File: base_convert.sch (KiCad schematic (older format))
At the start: 14 parts, among them J1 ISP, J2 DEBUG, Q1 Q_PMOS_GSD, SW2 SELECT, U1 MIC5317-3.3YM5-TR, U2 MSP430FR2033IPMR

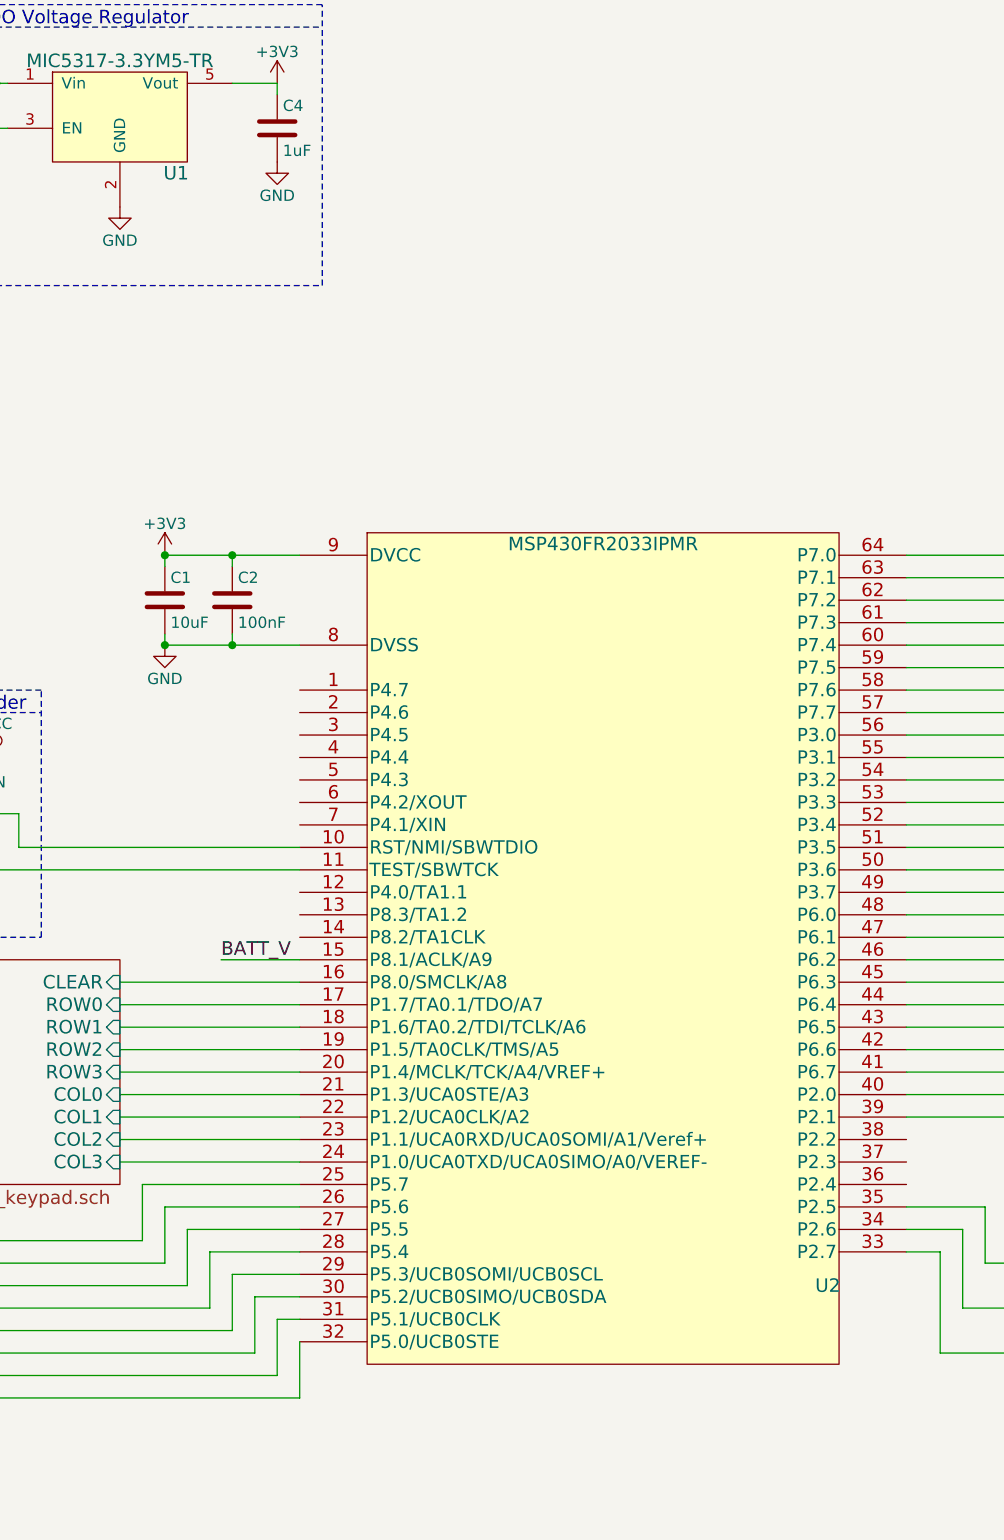
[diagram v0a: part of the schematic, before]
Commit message: spaw reference so U1 is uC as in previous version
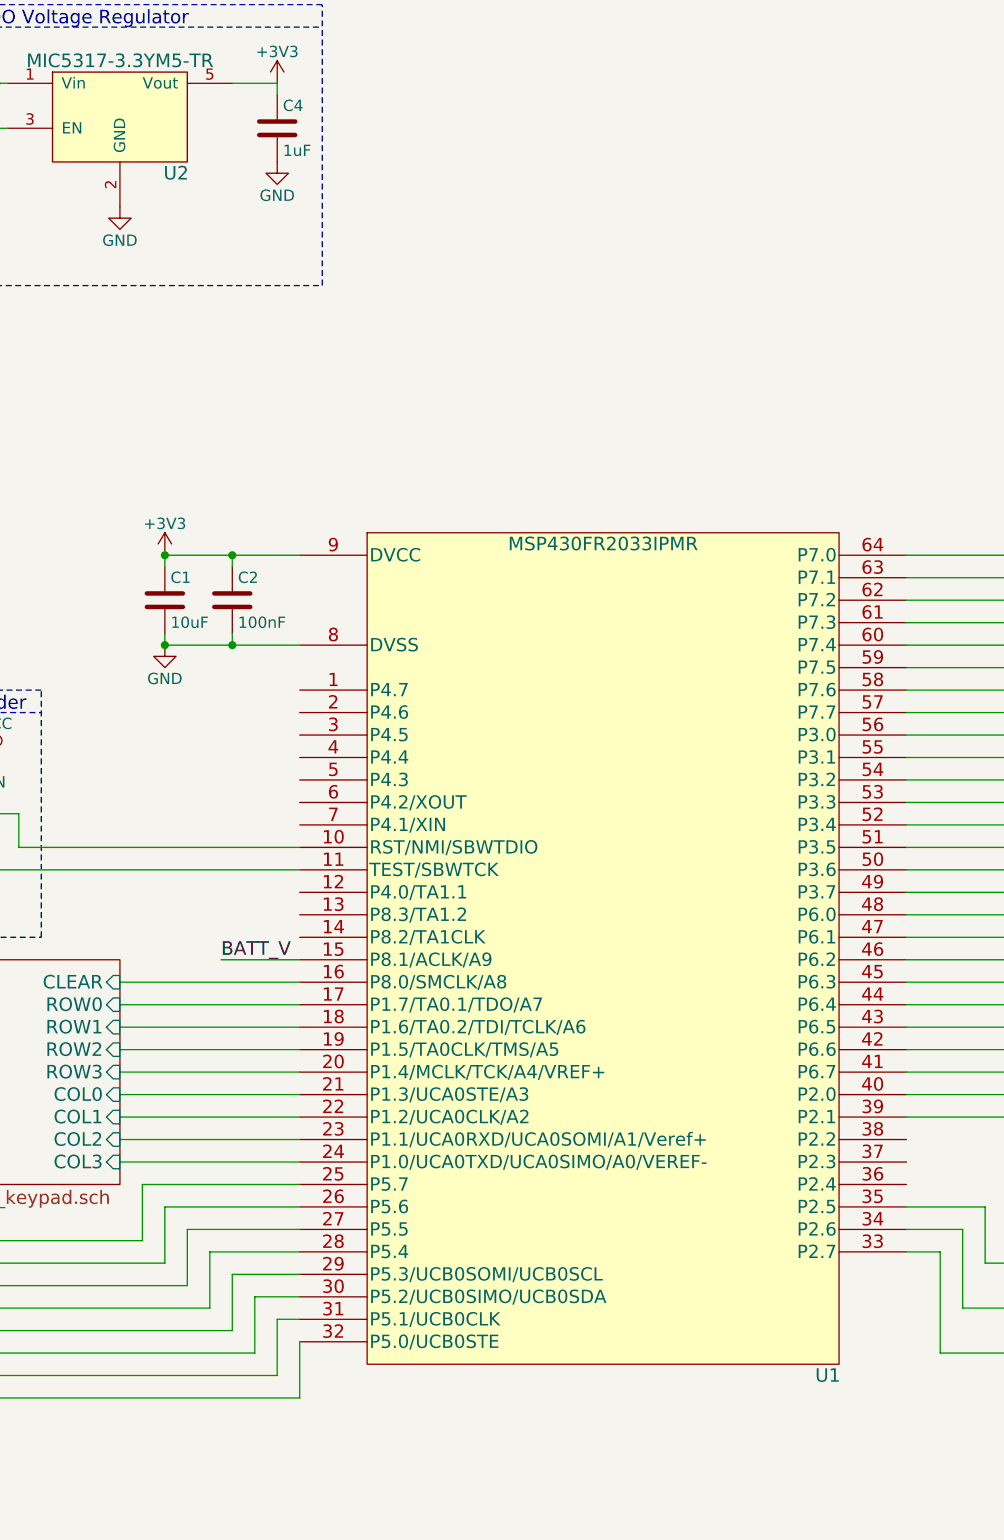
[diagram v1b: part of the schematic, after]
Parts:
- renumbered U2 to U1, U1 to U2
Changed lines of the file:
@@
 $EndComp
 $Comp
-L MSP430FR2033IPMR U2
+L MSP430FR2033IPMR U1
 U 1 1 5B2ADB04
 P 5050 3000
-F 0 "U2" H 7400 -250 60  0000 C CNN
+F 0 "U1" H 7400 -650 60  0000 C CNN
 F 1 "MSP430FR2033IPMR" H 6400 3050 60  0000 C CNN
 F 2 "Housings_QFP:LQFP-64_10x10mm_Pitch0.5mm" H 6400 3150 60  0001 C CNN
@@
 $EndComp
 $Comp
-L MIC5317 U1
+L MIC5317 U2
 U 1 1 5B283B2B
 P 4250 900
-F 0 "U1" H 4500 500 60  0000 C CNN
+F 0 "U2" H 4500 500 60  0000 C CNN
 F 1 "MIC5317-3.3YM5-TR" H 4250 1000 60  0000 C CNN
 F 2 "TO_SOT_Packages_SMD:SOT-23-5" H 4250 900 60  0001 C CNN
 F 3 "http://www.microchip.com/mymicrochip/filehandler.aspx?ddocname=en579427" H 4250 900 60  0001 C CNN
-F 4 "IC REG LINEAR 3.3V 150MA SOT23-5" H 4250 900 60  0001 C CNN "Description"
-F 5 "Microchip Technology" H 4250 900 60  0001 C CNN "Manufacture"
-F 6 "MIC5317-3.3YM5-TR" H 4250 900 60  0001 C CNN "Mfg Part Number"
-F 7 "SOT23-5" H 4250 900 60  0001 C CNN "Package"
+F 4 "Microchip Technology" H 4250 900 60  0001 C CNN "Manufacture"
+F 5 "MIC5317-3.3YM5-TR" H 4250 900 60  0001 C CNN "Mfg Part Number"
+F 6 "SOT23-5" H 4250 900 60  0001 C CNN "Package"
+F 7 "IC REG LINEAR 3.3V 150MA SOT23-5" H 4250 900 60  0001 C CNN "Description"
 	1    4250 900
 	1    0    0    -1

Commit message: reannotate schematic
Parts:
- renumbered C3 to C1, C1 to C2, C2 to C3, SW2 to SW1, U2 to U1, U1 to U2
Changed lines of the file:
@@
 $EndComp
 $Comp
-L GND #PWR01
+L GND #PWR3
 U 1 1 5AEC3D6F
 P 800 1600
-F 0 "#PWR01" H 800 1350 50  0001 C CNN
+F 0 "#PWR3" H 800 1350 50  0001 C CNN
 F 1 "GND" H 800 1450 50  0000 C CNN
 F 2 "" H 800 1600 50  0001 C CNN
@@
 $EndComp
 $Comp
-L GND #PWR02
+L GND #PWR4
 U 1 1 5AEC5CE6
 P 1550 1600
-F 0 "#PWR02" H 1550 1350 50  0001 C CNN
+F 0 "#PWR4" H 1550 1350 50  0001 C CNN
 F 1 "GND" H 1550 1450 50  0000 C CNN
 F 2 "" H 1550 1600 50  0001 C CNN
@@
 $EndComp
 $Comp
-L GND #PWR03
+L GND #PWR12
 U 1 1 5AF08A85
 P 4450 3400
-F 0 "#PWR03" H 4450 3150 50  0001 C CNN
+F 0 "#PWR12" H 4450 3150 50  0001 C CNN
 F 1 "GND" H 4450 3250 50  0000 C CNN
 F 2 "" H 4450 3400 50  0001 C CNN
@@
 $EndComp
 $Comp
-L C C1
+L C C2
 U 1 1 5AF0952E
 P 4450 3200
-F 0 "C1" H 4475 3300 50  0000 L CNN
+F 0 "C2" H 4475 3300 50  0000 L CNN
 F 1 "10uF" H 4475 3100 50  0000 L CNN
 F 2 "Capacitors_SMD:C_0805" H 4488 3050 50  0001 C CNN
@@
 $EndComp
 $Comp
-L C C2
+L C C3
 U 1 1 5AF09685
 P 4750 3200
-F 0 "C2" H 4775 3300 50  0000 L CNN
+F 0 "C3" H 4775 3300 50  0000 L CNN
 F 1 "100nF" H 4775 3100 50  0000 L CNN
 F 2 "Capacitors_SMD:C_0805" H 4788 3050 50  0001 C CNN
@@
 $EndComp
 $Comp
-L SS-24E06-TG5P SW2
-U 2 1 5AF1B232
+L SS-24E06-TG5P SW1
+U 1 1 5AF1B232
 P 2700 1100
-F 0 "SW2" H 2700 1470 50  0000 C CNN
+F 0 "SW1" H 2700 1470 50  0000 C CNN
 F 1 "SELECT" H 2700 700 50  0000 C CNN
 F 2 "Switch_CK:DP4T_SS-24E06-TG5P" H 2700 1300 50  0001 C CNN
@@
 F 6 "SS-24E06-TG 5 (P)" H 2700 1570 50  0001 C CNN "Mfg Part Number"
 F 7 "PC Pin" H 2700 1570 50  0001 C CNN "Package"
-	2    2700 1100
-	1    0    0    -1
-$EndComp
-$Comp
-L SS-24E06-TG5P SW2
-U 1 1 5AF1B53D
+	1    2700 1100
+	1    0    0    -1
+$EndComp
+$Comp
+L SS-24E06-TG5P SW1
+U 2 1 5AF1B53D
 P 9750 6250
-F 0 "SW2" H 9750 6620 50  0000 C CNN
+F 0 "SW1" H 9750 6620 50  0000 C CNN
 F 1 "SELECT" H 9750 5850 50  0000 C CNN
 F 2 "Switch_CK:DP4T_SS-24E06-TG5P" H 9750 6450 50  0001 C CNN
@@
 F 6 "SS-24E06-TG 5 (P)" H 9750 6720 50  0001 C CNN "Mfg Part Number"
 F 7 "PC Pin" H 9750 6720 50  0001 C CNN "Package"
-	1    9750 6250
+	2    9750 6250
 	-1   0    0    -1
 $EndComp
 $Comp
-L GND #PWR04
+L GND #PWR15
 U 1 1 5AF24AED
 P 10200 6500
-F 0 "#PWR04" H 10200 6250 50  0001 C CNN
+F 0 "#PWR15" H 10200 6250 50  0001 C CNN
 F 1 "GND" H 10200 6350 50  0000 C CNN
 F 2 "" H 10200 6500 50  0001 C CNN
@@
 $EndComp
 $Comp
-L GND #PWR05
+L GND #PWR2
 U 1 1 5AF3048A
 P 750 2950
-F 0 "#PWR05" H 750 2700 50  0001 C CNN
+F 0 "#PWR2" H 750 2700 50  0001 C CNN
 F 1 "GND" H 750 2800 50  0000 C CNN
 F 2 "" H 750 2950 50  0001 C CNN
@@
 $EndComp
 $Comp
-L GND #PWR06
+L GND #PWR6
 U 1 1 5AF42179
 P 3450 4500
-F 0 "#PWR06" H 3450 4250 50  0001 C CNN
+F 0 "#PWR6" H 3450 4250 50  0001 C CNN
 F 1 "GND" H 3450 4350 50  0000 C CNN
 F 2 "" H 3450 4500 50  0001 C CNN
@@
 $EndComp
 $Comp
-L VCC #PWR07
+L VCC #PWR9
 U 1 1 5AF43264
 P 3700 3900
-F 0 "#PWR07" H 3700 3750 50  0001 C CNN
+F 0 "#PWR9" H 3700 3750 50  0001 C CNN
 F 1 "VCC" H 3700 4050 50  0000 C CNN
 F 2 "" H 3700 3900 50  0001 C CNN
@@
 $EndComp
 $Comp
-L C C3
+L C C1
 U 1 1 5B284652
 P 3550 1100
-F 0 "C3" H 3575 1200 50  0000 L CNN
+F 0 "C1" H 3575 1200 50  0000 L CNN
 F 1 "1uF" H 3575 1000 50  0000 L CNN
 F 2 "Capacitors_SMD:C_0805" H 3588 950 50  0001 C CNN
@@
 $EndComp
 $Comp
-L GND #PWR08
+L GND #PWR8
 U 1 1 5B285DA8
 P 3550 1250
-F 0 "#PWR08" H 3550 1000 50  0001 C CNN
+F 0 "#PWR8" H 3550 1000 50  0001 C CNN
 F 1 "GND" H 3550 1100 50  0000 C CNN
 F 2 "" H 3550 1250 50  0001 C CNN
@@
 $EndComp
 $Comp
-L GND #PWR09
+L GND #PWR10
 U 1 1 5B285FB6
 P 4250 1450
-F 0 "#PWR09" H 4250 1200 50  0001 C CNN
+F 0 "#PWR10" H 4250 1200 50  0001 C CNN
 F 1 "GND" H 4250 1300 50  0000 C CNN
 F 2 "" H 4250 1450 50  0001 C CNN
@@
 $EndComp
 $Comp
-L GND #PWR010
+L GND #PWR14
 U 1 1 5B286569
 P 4950 1250
-F 0 "#PWR010" H 4950 1000 50  0001 C CNN
+F 0 "#PWR14" H 4950 1000 50  0001 C CNN
 F 1 "GND" H 4950 1100 50  0000 C CNN
 F 2 "" H 4950 1250 50  0001 C CNN
@@
 $EndComp
 $Comp
-L VCC #PWR011
+L VCC #PWR1
 U 1 1 5B28B1DA
 P 750 2200
-F 0 "#PWR011" H 750 2050 50  0001 C CNN
+F 0 "#PWR1" H 750 2050 50  0001 C CNN
 F 1 "VCC" H 750 2350 50  0000 C CNN
 F 2 "" H 750 2200 50  0001 C CNN
@@
 $EndComp
 $Comp
-L +3V3 #PWR012
+L +3V3 #PWR13
 U 1 1 5B28D631
 P 4950 900
-F 0 "#PWR012" H 4950 750 50  0001 C CNN
+F 0 "#PWR13" H 4950 750 50  0001 C CNN
 F 1 "+3V3" H 4950 1040 50  0000 C CNN
 F 2 "" H 4950 900 50  0001 C CNN
@@
 $EndComp
 $Comp
-L VCC #PWR013
+L VCC #PWR5
 U 1 1 5B29E8A8
 P 3200 850
-F 0 "#PWR013" H 3200 700 50  0001 C CNN
+F 0 "#PWR5" H 3200 700 50  0001 C CNN
 F 1 "VCC" H 3200 1000 50  0000 C CNN
 F 2 "" H 3200 850 50  0001 C CNN
@@
 $EndComp
 $Comp
-L +3V3 #PWR014
+L +3V3 #PWR11
 U 1 1 5B2A0C6B
 P 4450 3000
-F 0 "#PWR014" H 4450 2850 50  0001 C CNN
+F 0 "#PWR11" H 4450 2850 50  0001 C CNN
 F 1 "+3V3" H 4450 3140 50  0000 C CNN
 F 2 "" H 4450 3000 50  0001 C CNN
@@
 $EndComp
 $Comp
-L MSP430FR2033IPMR U1
+L MSP430FR2033IPMR U2
 U 1 1 5B2ADB04
 P 5050 3000
-F 0 "U1" H 7400 -650 60  0000 C CNN
+F 0 "U2" H 7400 -650 60  0000 C CNN
 F 1 "MSP430FR2033IPMR" H 6400 3050 60  0000 C CNN
 F 2 "Housings_QFP:LQFP-64_10x10mm_Pitch0.5mm" H 6400 3150 60  0001 C CNN
@@
 $EndComp
 $Comp
-L MIC5317 U2
+L MIC5317 U1
 U 1 1 5B283B2B
 P 4250 900
-F 0 "U2" H 4500 500 60  0000 C CNN
+F 0 "U1" H 4500 500 60  0000 C CNN
 F 1 "MIC5317-3.3YM5-TR" H 4250 1000 60  0000 C CNN
 F 2 "TO_SOT_Packages_SMD:SOT-23-5" H 4250 900 60  0001 C CNN
@@
 $EndComp
 $Comp
-L GND #PWR015
+L GND #PWR7
 U 1 1 5B2882B1
 P 3450 7100
-F 0 "#PWR015" H 3450 6850 50  0001 C CNN
+F 0 "#PWR7" H 3450 6850 50  0001 C CNN
 F 1 "GND" H 3450 6950 50  0000 C CNN
 F 2 "" H 3450 7100 50  0001 C CNN

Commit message: battery clip change to wire connection
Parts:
- added J3: Vin, Connectors_JST:JST_PH_S2B-PH-K_02x2.00mm_Angled, symbol Conn_01x02
- BT1: value 4 Cell AA Battery Holder -> 4 Cell AA Battery Clip; footprint MPD:BC4AAPC -> MPD:BC4AAW; symbol Battery -> BC4AAW; Description HOLDER BATT 4-AA CELLS PC MNT -> HOLDER BATT 4-AA CELLS WIRE LDS; Mfg Part Number BC4AAPC -> BC4AAW; Package PC Pin -> Wire
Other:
- note added: "Battery Clip Wire \nto JST Connector"
- moved on the sheet: C1, C4, Q1, SW1A, U1

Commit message: make erc happy
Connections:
- no-connect marks 2 -> 15
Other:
- note added: "Make ERC Happy"
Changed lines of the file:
@@
 EESchema Schematic File Version 2
-LIBS:base_convert-cache
 LIBS:Display_LiteOn
 LIBS:MSP430
@@
 LIBS:Connector_Generic
 LIBS:MPD_BatteryClip
+LIBS:base_convert-cache
 EELAYER 25 0
 EELAYER END
@@
 Sheet 1 4
 Title "Base Convert"
-Date "2018-06-18"
+Date "2018-06-20"
 Rev "A"
 Comp "Perry Leumas"
@@
 	1900 1600 1900 1400
 Wire Wire Line
-	4450 3000 5050 3000
+	4450 3000 4750 3000
+Wire Wire Line
+	4750 3000 5050 3000
 Wire Wire Line
 	4450 3000 4450 3050
@@
 	4450 3350 4450 3400
 Wire Wire Line
-	4450 3400 5050 3400
+	4450 3400 4750 3400
+Wire Wire Line
+	4750 3400 5050 3400
 Wire Wire Line
 	3400 1400 3250 1400
@@
 	750  2950 750  2900
 Wire Wire Line
-	750  2500 750  2600
+	750  2500 750  2550
+Wire Wire Line
+	750  2550 750  2600
 Wire Wire Line
 	750  2550 1150 2550
@@
 	4100 1100 4050 1100
 Wire Wire Line
-	4050 900  4050 1100
+	4050 1100 4050 900
 Wire Wire Line
 	5100 900  5300 900
@@
 	5300 900  5300 950
 Wire Wire Line
-	3400 1000 3400 1400
+	3400 1000 3400 1200
+Wire Wire Line
+	3400 1200 3400 1400
 Wire Wire Line
 	3300 4050 3300 3950
@@
 	2950 3700 3900 3700
 Wire Wire Line
-	3550 1000 3250 1000
-Wire Wire Line
-	3550 900  4100 900
+	3550 1000 3400 1000
+Wire Wire Line
+	3400 1000 3250 1000
+Wire Wire Line
+	3550 900  3900 900
+Wire Wire Line
+	3900 900  4050 900
+Wire Wire Line
+	4050 900  4100 900
 Wire Notes Line
 	3750 550  3750 1800
@@
 	2800 650  3650 650
 Wire Wire Line
-	3550 850  3550 1000
+	3550 850  3550 900
+Wire Wire Line
+	3550 900  3550 1000
 Wire Wire Line
 	4750 3400 4750 3350
@@
 	5050 6750 5050 6500
 Wire Wire Line
-	3450 6850 3450 7100
+	3450 6850 3450 6950
+Wire Wire Line
+	3450 6950 3450 7100
 Wire Wire Line
 	3450 6850 3300 6850
@@
 Text Notes 650  1750 0    50   ~ 0
 Battery Clip Wire \nto JST Connector
+NoConn ~ 5050 3600
+NoConn ~ 5050 3700
+NoConn ~ 5050 3800
+NoConn ~ 5050 3900
+NoConn ~ 5050 4000
+NoConn ~ 5050 4100
+NoConn ~ 5050 4200
+NoConn ~ 5050 4500
+NoConn ~ 5050 4600
+NoConn ~ 5050 4700
+NoConn ~ 7750 5600
+NoConn ~ 7750 5700
+NoConn ~ 7750 5800
+$Comp
+L PWR_FLAG #FLG016
+U 1 1 5B2BCABB
+P 750 7750
+F 0 "#FLG016" H 750 7825 50  0001 C CNN
+F 1 "PWR_FLAG" H 750 7900 50  0000 C CNN
+F 2 "" H 750 7750 50  0001 C CNN
+F 3 "" H 750 7750 50  0001 C CNN
+	1    750  7750
+	1    0    0    -1
+$EndComp
+$Comp
+L GND #PWR017
+U 1 1 5B2BCBCF
+P 750 7750
+F 0 "#PWR017" H 750 7500 50  0001 C CNN
+F 1 "GND" H 750 7600 50  0000 C CNN
+F 2 "" H 750 7750 50  0001 C CNN
+F 3 "" H 750 7750 50  0001 C CNN
+	1    750  7750
+	1    0    0    -1
+$EndComp
+Text Notes 550  7500 0    60   ~ 0
+Make ERC Happy
+Wire Notes Line
+	550  7400 550  7950
+Wire Notes Line
+	550  7950 1450 7950
+Wire Notes Line
+	1450 7950 1450 7400
+Wire Notes Line
+	1450 7400 550  7400
+Wire Notes Line
+	550  7500 1450 7500
+$Comp
+L VCC #PWR018
+U 1 1 5B2C495B
+P 1200 7750
+F 0 "#PWR018" H 1200 7600 50  0001 C CNN
+F 1 "VCC" H 1200 7900 50  0000 C CNN
+F 2 "" H 1200 7750 50  0001 C CNN
+F 3 "" H 1200 7750 50  0001 C CNN
+	1    1200 7750
+	-1   0    0    1
+$EndComp
+$Comp
+L PWR_FLAG #FLG019
+U 1 1 5B2C4DB7
+P 1200 7750
+F 0 "#FLG019" H 1200 7825 50  0001 C CNN
+F 1 "PWR_FLAG" H 1200 7900 50  0000 C CNN
+F 2 "" H 1200 7750 50  0001 C CNN
+F 3 "" H 1200 7750 50  0001 C CNN
+	1    1200 7750
+	1    0    0    -1
+$EndComp
 $EndSCHEMATC
